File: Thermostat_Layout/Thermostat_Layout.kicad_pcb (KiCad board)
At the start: 2 copper layers, 52 parts, among them J1 Conn_01x03, J2 Conn_01x03, J3 Conn_01x02_Male, J4 Conn_01x04, J5 Conn_01x10, J6 LCD_HEADER, J7 Conn_01x03, J8 Conn_01x03, SW1 SW_Push, SW2 SW_SPST, SW3 SW_SPST, SW4 SW_DPDT_x2, U1 LM50CIM3, U2 ATMEGA328P-AU, U3 TSR_1-2433, U4 TLP3545, U5 MCP23017_SO, U6 TLP3545, U7 TLP3545, U8 DS3231MZ, U9 ESP-07, Y1 Crystal

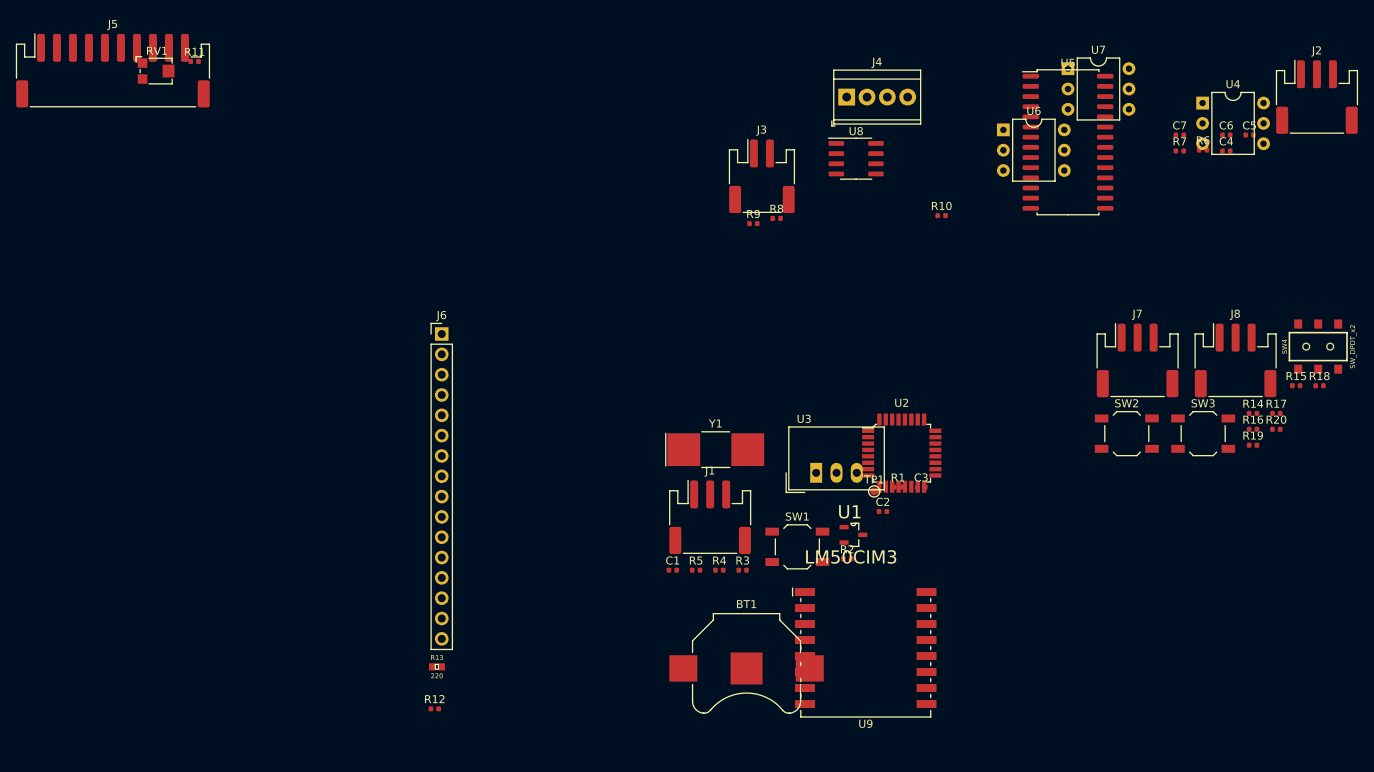
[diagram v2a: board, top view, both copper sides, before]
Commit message: Schematic and PCB layout for thermostat
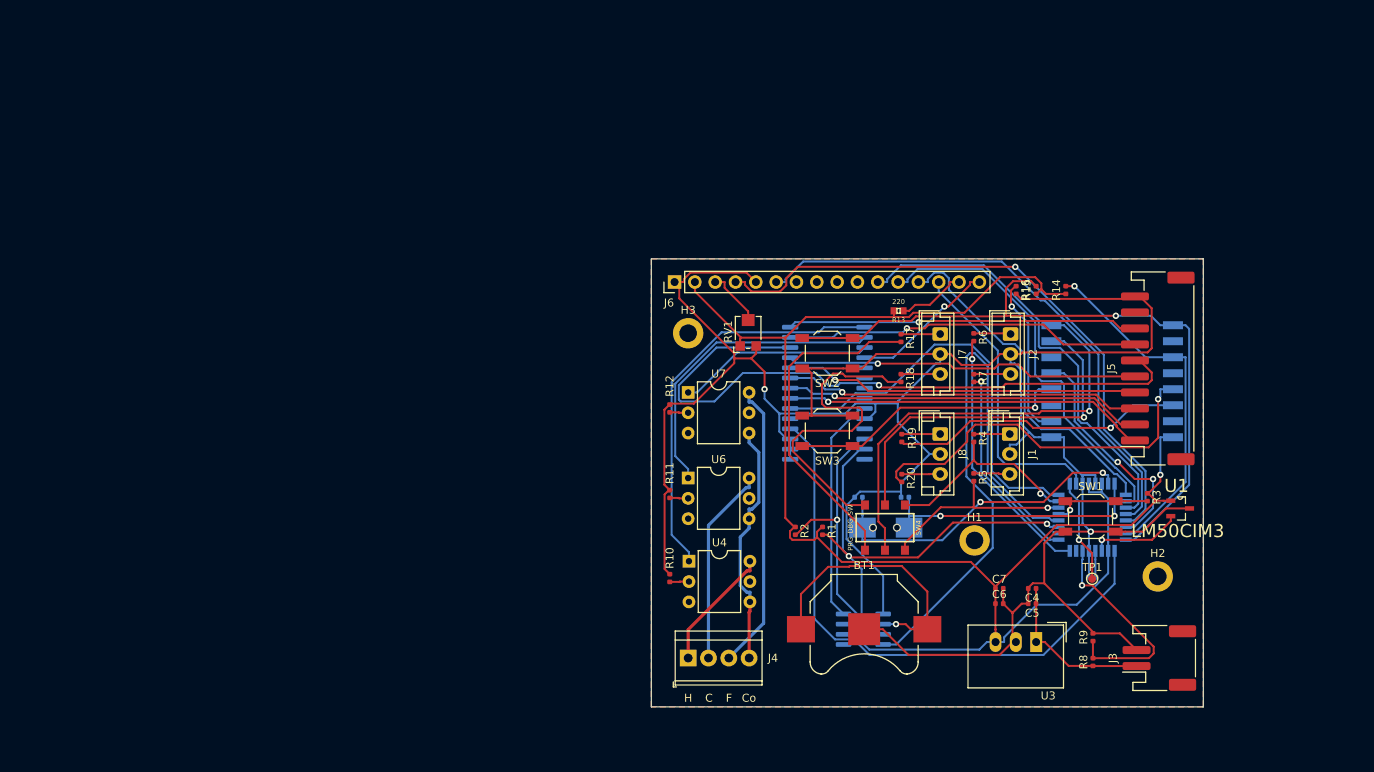
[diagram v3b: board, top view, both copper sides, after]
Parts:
- added H1: MountingHole, MountingHole:MountingHole_2.2mm_M2_DIN965_Pad, F.Cu at (156.1, 102.7)
- added H2: MountingHole, MountingHole:MountingHole_2.2mm_M2_DIN965_Pad, F.Cu at (179.0, 107.2)
- added H3: MountingHole, MountingHole:MountingHole_2.2mm_M2_DIN965_Pad, F.Cu at (120.3, 76.8)
- C1, C2, C3, U2, U5, U8, U9: moved to B.Cu
- J1: value Conn_01x03 -> UC_PRG; footprint Connector_JST:JST_PH_S3B-PH-SM4-TB_1x03-1MP_P2.00mm_Horizontal -> Connector_JST:JST_EH_B3B-EH-A_1x03_P2.50mm_Vertical
- J2: value Conn_01x03 -> UC_DBG; footprint Connector_JST:JST_PH_S3B-PH-SM4-TB_1x03-1MP_P2.00mm_Horizontal -> Connector_JST:JST_EH_B3B-EH-A_1x03_P2.50mm_Vertical
- J3: value Conn_01x02_Male -> VIN
- J4: value Conn_01x04 -> HVAC_HEADER
- J5: value Conn_01x10 -> BTN_HEADER
- J7: value Conn_01x03 -> RF_PRG; footprint Connector_JST:JST_PH_S3B-PH-SM4-TB_1x03-1MP_P2.00mm_Horizontal -> Connector_JST:JST_EH_B3B-EH-A_1x03_P2.50mm_Vertical
- J8: value Conn_01x03 -> RF_DBG; footprint Connector_JST:JST_PH_S3B-PH-SM4-TB_1x03-1MP_P2.00mm_Horizontal -> Connector_JST:JST_EH_B3B-EH-A_1x03_P2.50mm_Vertical
- RV1: value R_POT_US -> LCD_CONT
- SW2: value SW_SPST -> RF_RST
- SW3: value SW_SPST -> RF_PRG
- SW4: value SW_DPDT_x2 -> PRG_DBG_SW
- Y1: footprint Crystal:Crystal_SMD_SeikoEpson_MC405-2Pin_9.6x4.1mm -> Crystal:Crystal_SMD_0603-2Pin_6.0x3.5mm_HandSoldering; moved to B.Cu
- moved J5 135.8 mm to (179.0, 81.2), turned to 90 degrees
- moved U4 86.0 mm to (120.4, 105.3)
- moved RV1 80.8 mm to (127.8, 76.6), turned to 90 degrees
- moved R11 80.3 mm to (118.0, 96.9), turned to 90 degrees
- moved J3 78.1 mm to (179.2, 117.4), turned to 90 degrees
- moved J4 72.9 mm to (120.3, 117.4)
- moved R13 72.9 mm to (146.6, 74.0), turned to 180 degrees
- moved R8 68.1 mm to (170.9, 117.9), turned to 90 degrees
- moved R9 66.9 mm to (170.9, 114.8), turned to 90 degrees
- moved C6 65.1 mm to (159.2, 110.6)
- moved C5 64.6 mm to (163.3, 110.6), turned to 180 degrees
- moved U7 62.4 mm to (120.3, 84.2)
- moved C7 61.0 mm to (159.2, 108.7)
- moved C4 59.8 mm to (163.3, 108.7), turned to 180 degrees
- moved U8 58.8 mm to (142.2, 113.8)
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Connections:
- R8 pad 2: /Power/BATT_MON -> BATT_MON
- R9 pad 1: /Power/BATT_MON -> BATT_MON
- R9 pad 2: (no net) -> GND
- U2 pad 22: (no net) -> BATT_MON
- U5 pad 12: (no net) -> SCL
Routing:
- net GND: track 0.00 -> 339.4 mm, vias 0 -> 2
- net 3.3V: track 0.00 -> 241.0 mm, vias 0 -> 1
- net SCL: track 0.00 -> 108.1 mm, vias 0 -> 1
- net RADIO_RST: track 0.00 -> 88.3 mm, vias 0 -> 1
- net REMOTE_BTN: track 0.00 -> 83.4 mm, vias 0 -> 1
- net LCD_RS: track 0.00 -> 77.6 mm, vias 0 -> 1
- net EXP_RST: track 0.00 -> 72.5 mm
- net LCD_EN: track 0.00 -> 70.1 mm
- net SDA: track 0.00 -> 59.6 mm, vias 0 -> 2
- net LCD_D4: track 0.00 -> 55.8 mm
- net /Radio/TX: track 0.00 -> 55.3 mm, vias 0 -> 1
- net EXP_INT: track 0.00 -> 52.4 mm
- net LCD_D5: track 0.00 -> 50.9 mm
- net HEAT_ON: track 0.00 -> 50.2 mm
- net /Radio/DBG_RX: track 0.00 -> 46.9 mm, vias 0 -> 1
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- added copper zone on B.Cu, net GND
- added copper zone on F.Cu, net GND
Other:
- board outline added: 69 x 56 mm
- board text added: "C"
- board text added: "Co"
- board text added: "F"
- board text added: "H"

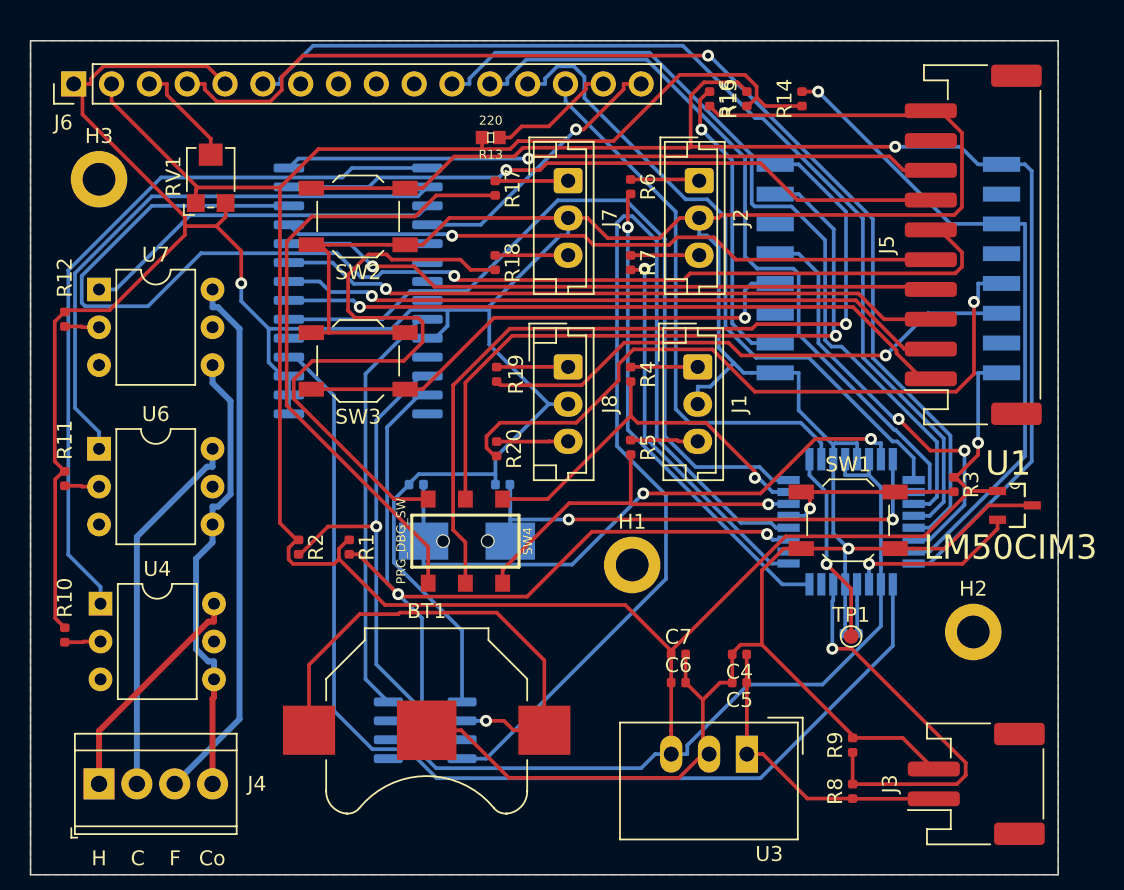
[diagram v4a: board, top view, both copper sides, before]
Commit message: Move some components around
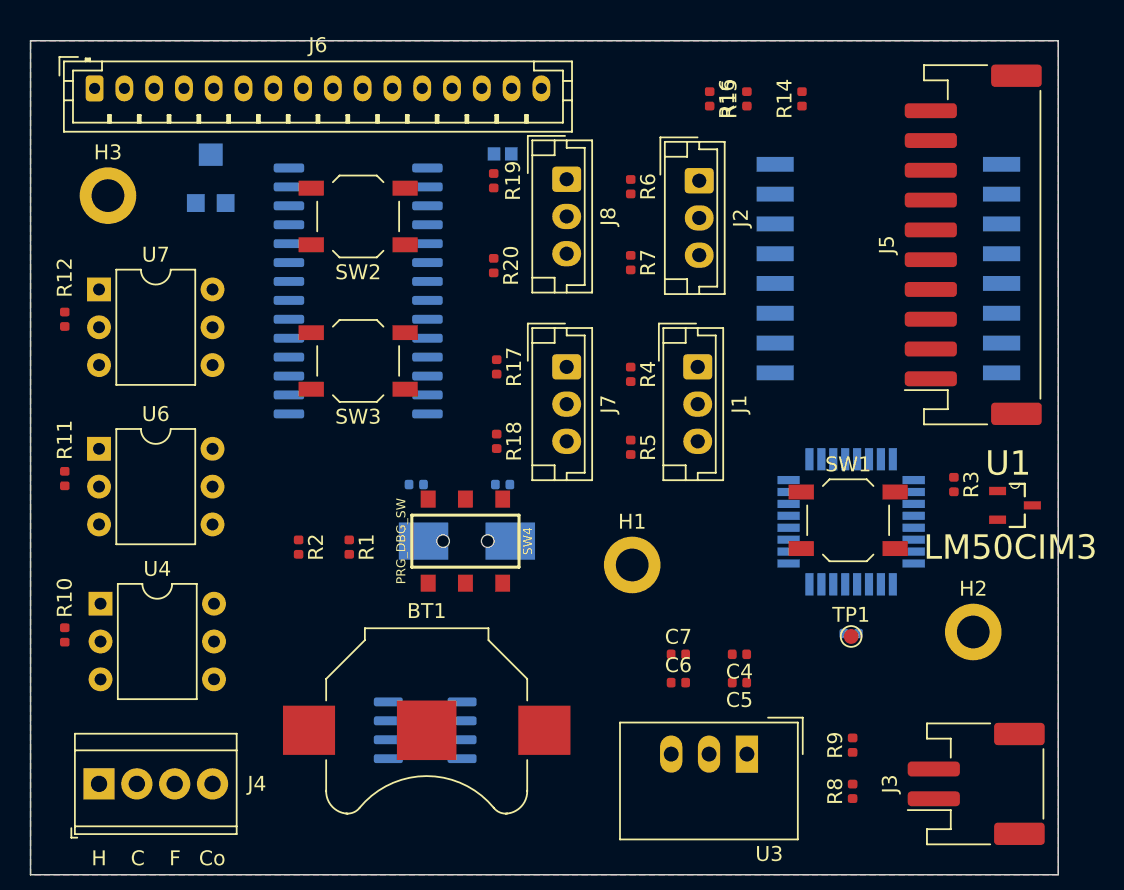
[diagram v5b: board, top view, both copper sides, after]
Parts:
- J6: footprint Connector_PinHeader_2.54mm:PinHeader_1x16_P2.54mm_Vertical -> Connector_JST:JST_PH_B16B-PH-K_1x16_P2.00mm_Vertical
- R13, RV1: moved to B.Cu
- moved R19 13.0 mm to (146.8, 76.9)
- moved J8 12.6 mm to (151.7, 76.8)
- moved J7 12.5 mm to (151.7, 89.4)
- moved R20 12.3 mm to (146.8, 82.6)
- moved R17 12.0 mm to (147.0, 89.4)
- moved R18 12.0 mm to (147.0, 94.4)
- moved J6 1.43 mm to (120.0, 70.7), turned to 0 degrees
- moved R13 1.36 mm to (147.4, 75.1)
- moved H3 1.25 mm to (120.9, 77.9)
- turned U8 to 180 degrees
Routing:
- net GND: track 339.4 -> 0.00 mm, vias 2 -> 0
- net 3.3V: track 241.0 -> 0.00 mm, vias 1 -> 0
- net SCL: track 108.1 -> 0.00 mm, vias 1 -> 0
- net RADIO_RST: track 88.3 -> 0.00 mm, vias 1 -> 0
- net REMOTE_BTN: track 83.4 -> 0.00 mm, vias 1 -> 0
- net LCD_RS: track 77.6 -> 0.00 mm, vias 1 -> 0
- net EXP_RST: track 72.5 -> 0.00 mm
- net LCD_EN: track 70.1 -> 0.00 mm
- net SDA: track 59.6 -> 0.00 mm, vias 2 -> 0
- net LCD_D4: track 55.8 -> 0.00 mm
- net /Radio/TX: track 55.3 -> 0.00 mm, vias 1 -> 0
- net EXP_INT: track 52.4 -> 0.00 mm
- net LCD_D5: track 50.9 -> 0.00 mm
- net HEAT_ON: track 50.2 -> 0.00 mm
- net /Radio/DBG_RX: track 46.9 -> 0.00 mm, vias 1 -> 0
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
